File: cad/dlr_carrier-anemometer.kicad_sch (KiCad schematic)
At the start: 9 parts, among them J13 ANEMO_M12_5P, U7 SP3485EN

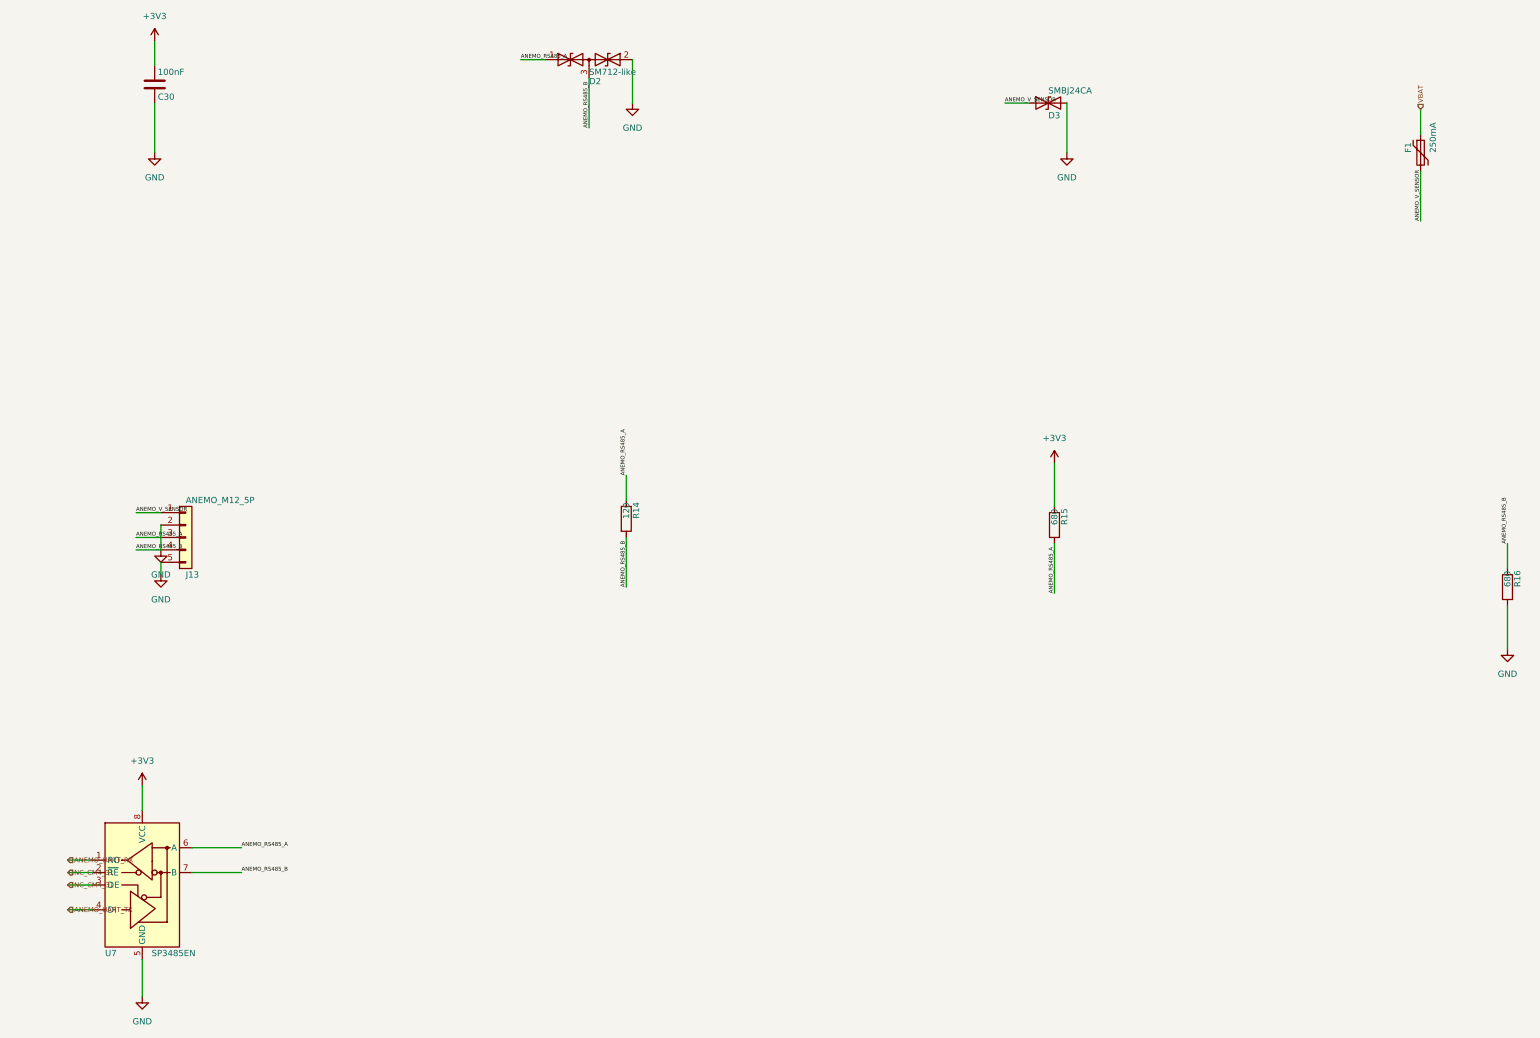
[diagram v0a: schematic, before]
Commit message: 🗺 feat(cad): scripted schematic + board pipeline, 4-layer stack
The committed board had almost every pad on +3V3 — no 5V_RAIL, VBAT or SDA1 net
existed on it at all — so the gerbers in output/ were never a valid board. Cause:
"Update PCB from Schematic" is GUI-only, so nothing kept the board honest, and the
schematic generator itself was merging nets.

Schematic generator:
  * power stubs now run along the pin direction; they used to be forced up or down
    regardless, which drove a 5V_RAIL stub straight through the buck inductor's
    BUCK_SW pin
  * PWR_FLAGs are placed by rule — any net that reaches a power-input pin with no
    power-output pin gets exactly one — instead of a hardcoded list, which is what
    the new VBAT and CHG_VCC rails needed
  * placement is deterministic; it used Python's salted hash(), so no two runs
    produced the same schematic
  * sch_guard fails the build on any cross-net wire/pin collision
  * ~700 lines of dead single-sheet generator removed
  ERC: 0 violations across all 8 sheets.

Board pipeline (cad/drawing/, all scripted, no GUI step):
  sync_pcb      rebuilds every footprint from the library and reassigns every pad
                net from the SKiDL netlist — the replacement for F8
  board_setup   4-layer SIG/GND/5V/SIG stack, rules, net classes, planes (ADR-016)
  route_pcb     DSN -> Freerouting -> SES, after patching the DSN so plane layers
                are "power" (the router was slicing the planes with signals) and
                the plane declarations are dropped (the router had been leaving
                GND and 5V pads with no path to the plane at all)
  stitch_planes vias from surface pads into their plane
  close_gaps    closes what the router leaves, using real segment-to-segment
                clearance; it never forces copper through another net

DRC: 265 unconnected -> 5, with no clearance, short, annular-ring or courtyard
errors. The remaining 5 are escapes on the DF40, the VQFN and the MSOP; they are
l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
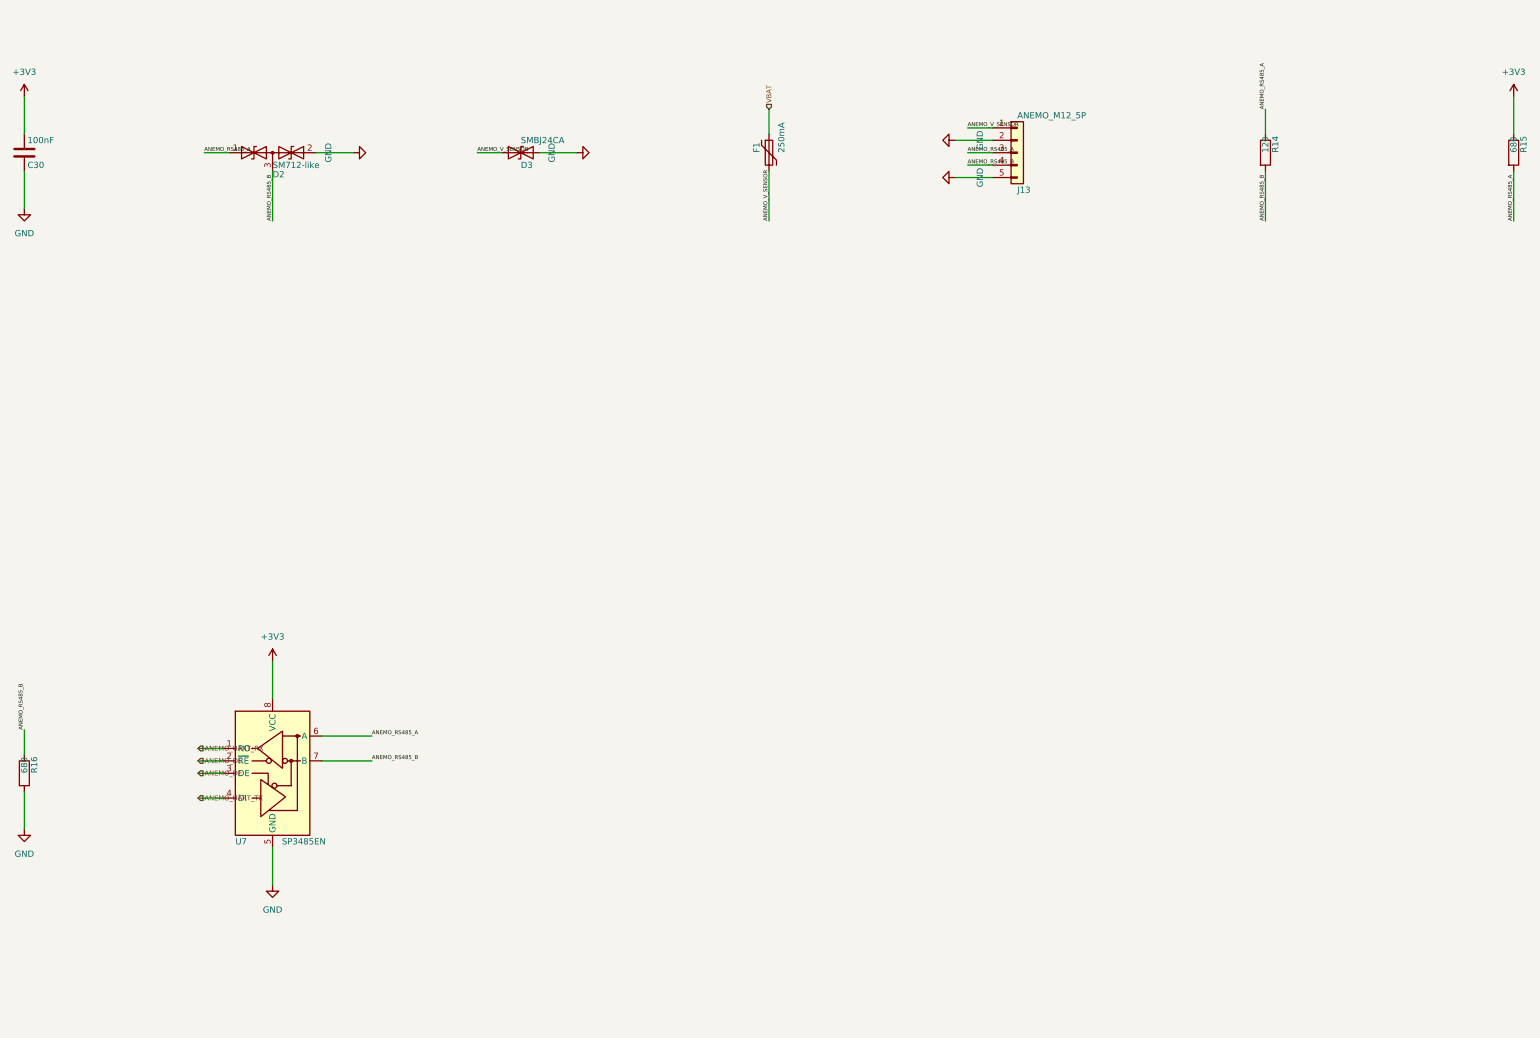
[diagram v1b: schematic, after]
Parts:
- D3: footprint Package_TO_SOT_SMD:SOT-23 -> Diode_SMD:D_SMB
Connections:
- net GND: no longer D2.3 (common), J13.4 (Pin_4), R14.2, R16.1, U7.7 (B)
- net NC_CM4_31 renamed ANEMO_DE
- new net ANEMO_RS485_B: D2.3 (common), J13.4 (Pin_4), R14.2, R16.1, U7.7 (B)

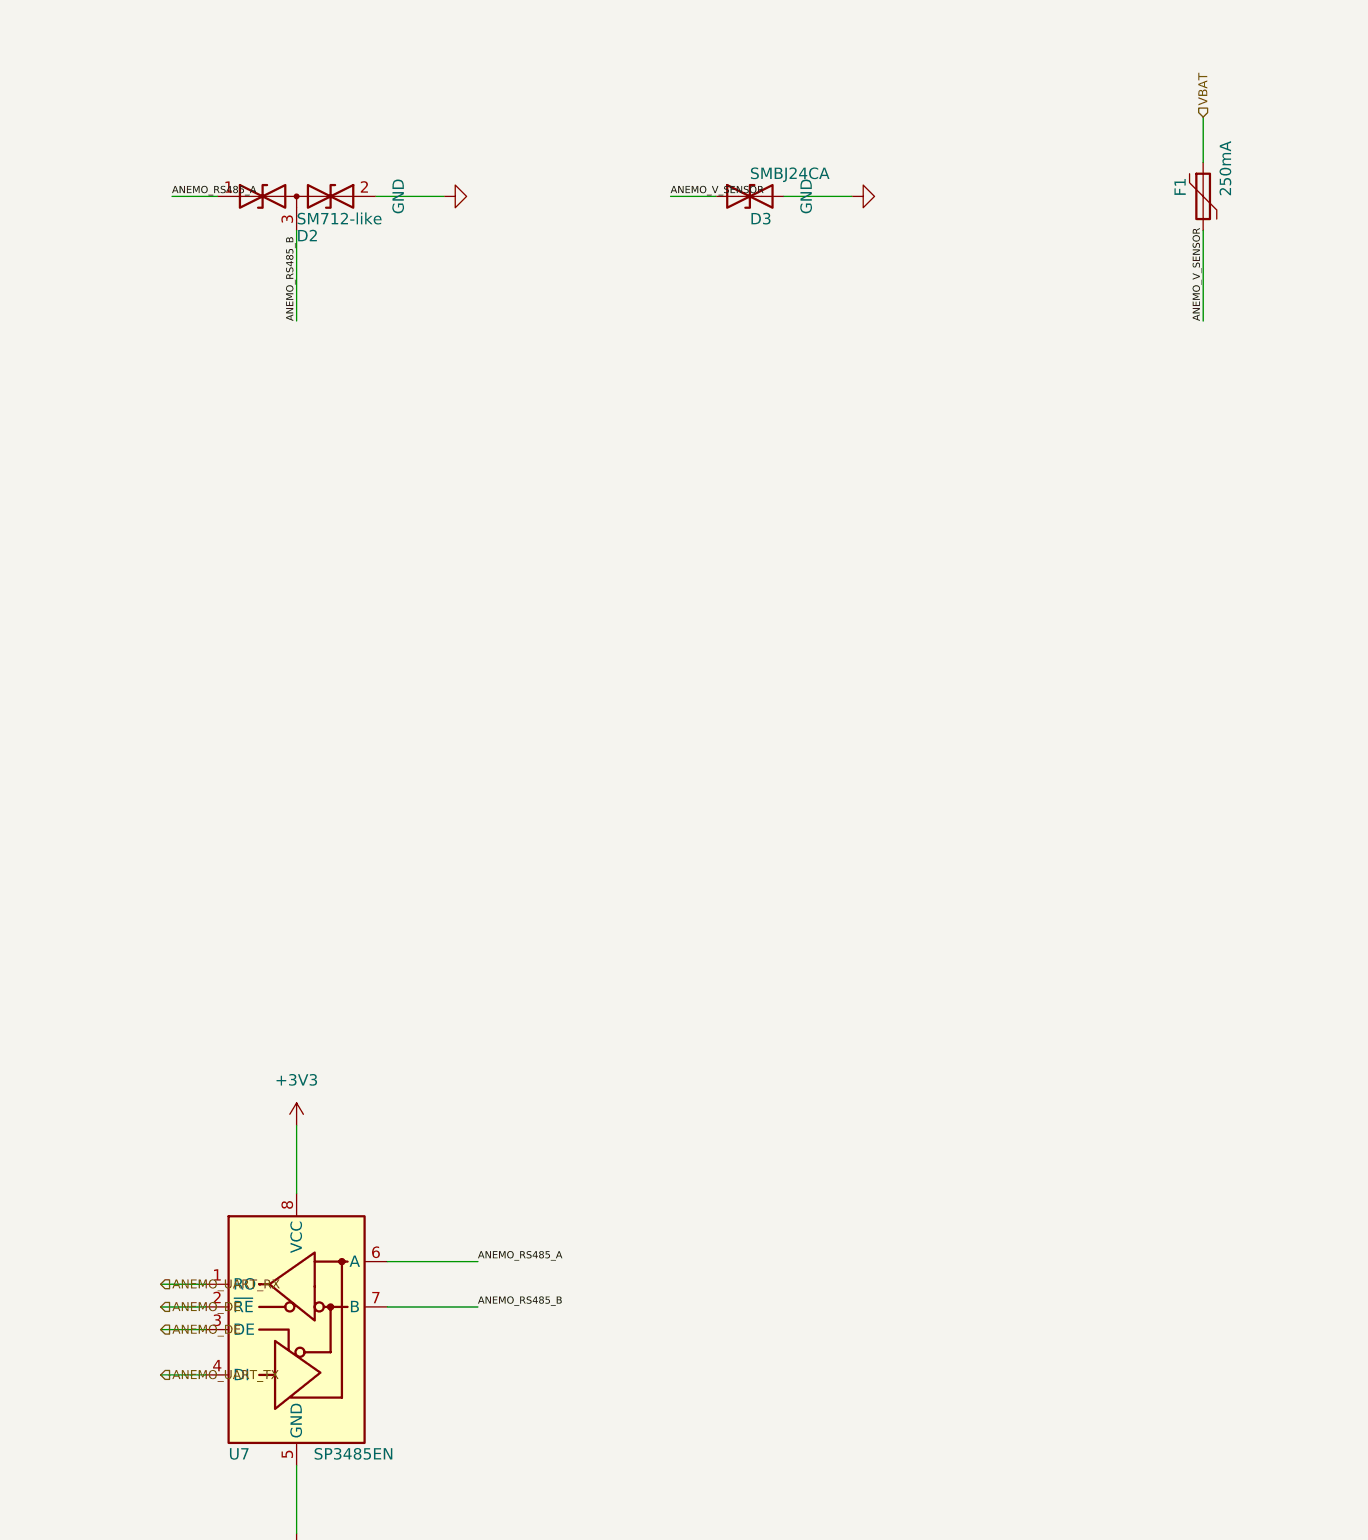
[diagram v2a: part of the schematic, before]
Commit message: 🩺 fix(schematic): match hierarchical label type to the sheet pin
The 117 KiCad 9 errors were a type mismatch, not the hierarchy metadata: every
child hierarchical label was written as `(shape input)` while the root's sheet pins
are bidirectional. KiCad's hier_label_mismatch check compares electrical type as
well as name, so on KiCad 9 every cross-sheet net failed, and the root labels then
read as dangling. KiCad 10 tolerates the mismatch, which is why it passed here.

kicad-sch-api 0.5.6 accepts a shape argument on add_hierarchical_label and ignores
it — the third serialization bug worked around in this generator — so the shape is
rewritten in the saved sheet.

Co-Authored-By: Claude Opus 5 <noreply@anthropic.com>
Claude-Session: https://claude.ai/code/session_011xr7VCL7rkJj2WE2uQF7sF
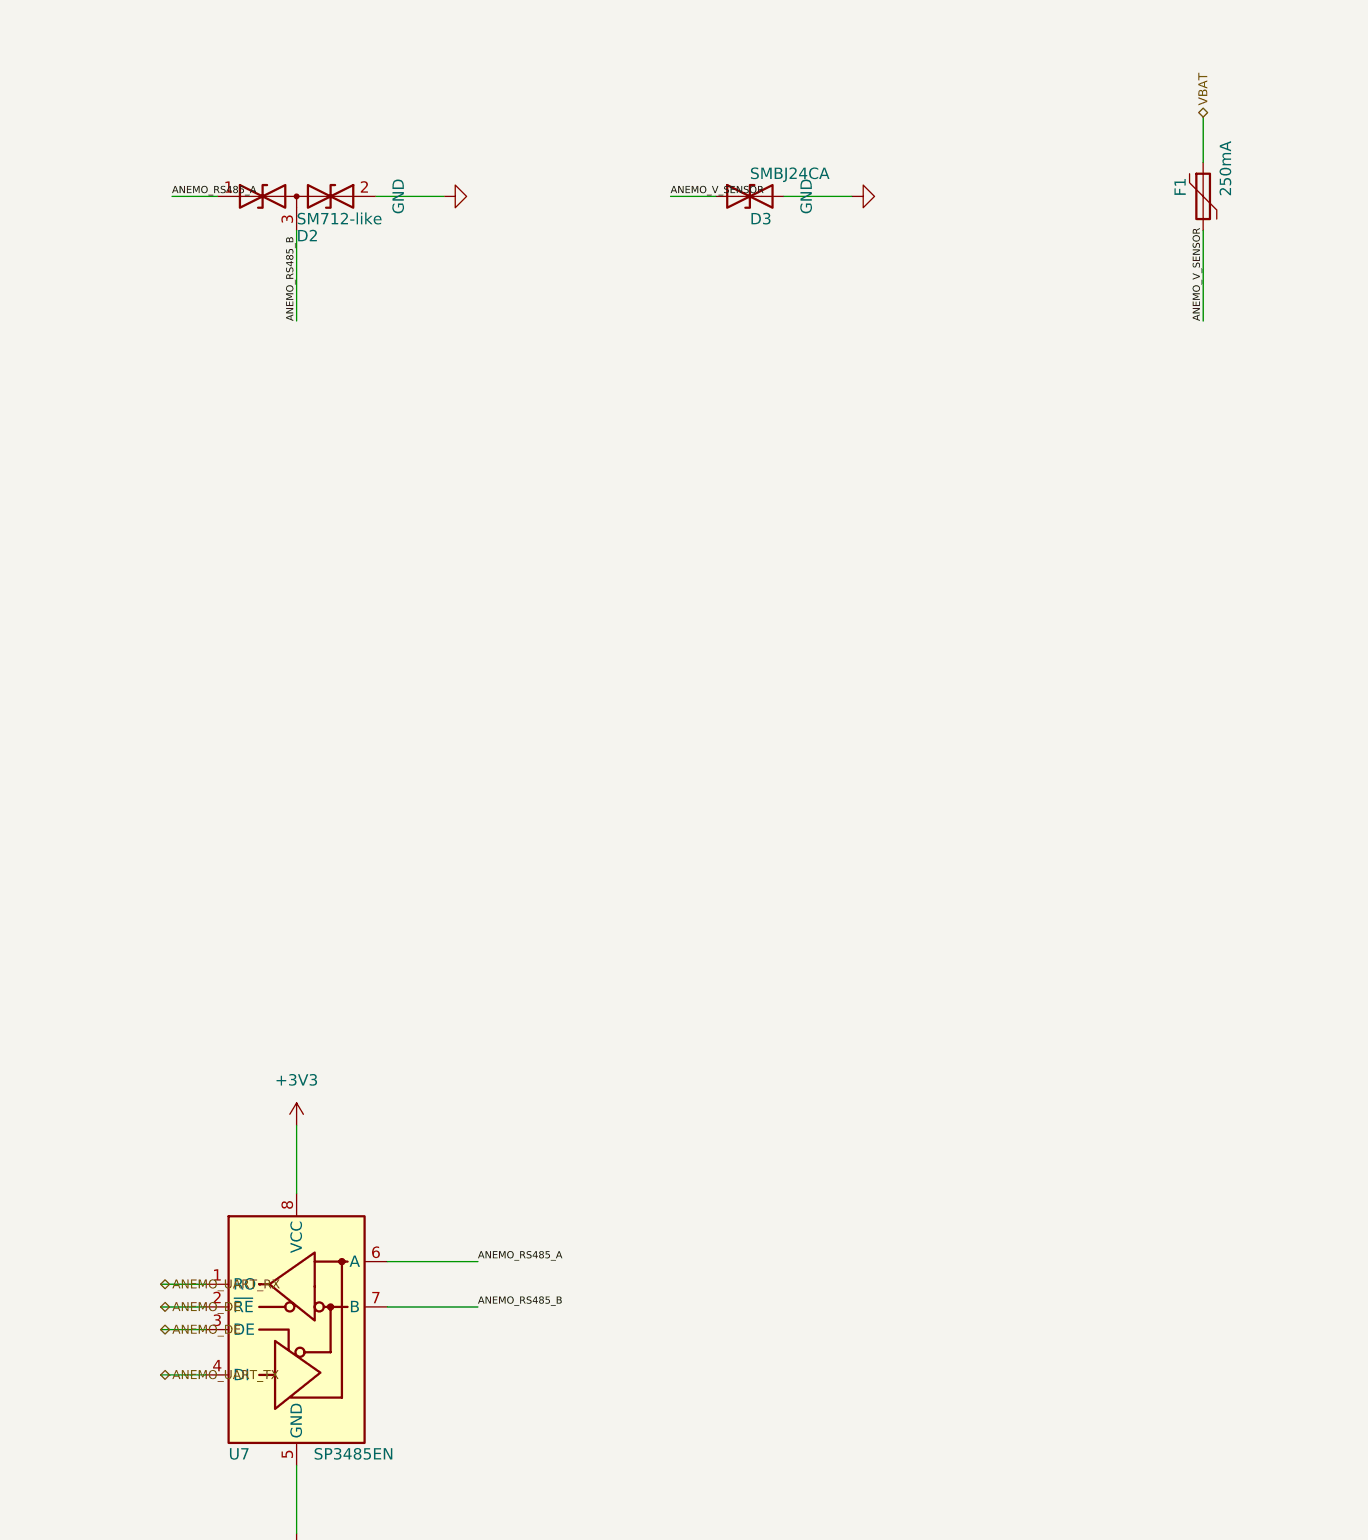
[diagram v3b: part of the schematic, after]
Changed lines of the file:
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@@
 		(instances
 			(project "ANEMOMETER RS-485"
-				(path "/006f20aa-e6de-45ca-869a-804cb883c933"
+				(path "/6472ff61-5240-4a8c-a1e1-c967d2308f1e"
 					(reference "C30")
 					(unit 1)
@@
 		(instances
 			(project "ANEMOMETER RS-485"
-				(path "/006f20aa-e6de-45ca-869a-804cb883c933"
+				(path "/6472ff61-5240-4a8c-a1e1-c967d2308f1e"
 					(reference "D2")
 					(unit 1)
@@
 		(instances
 			(project "ANEMOMETER RS-485"
-				(path "/006f20aa-e6de-45ca-869a-804cb883c933"
+				(path "/6472ff61-5240-4a8c-a1e1-c967d2308f1e"
 					(reference "D3")
 					(unit 1)
@@
 		(instances
 			(project "ANEMOMETER RS-485"
-				(path "/006f20aa-e6de-45ca-869a-804cb883c933"
+				(path "/6472ff61-5240-4a8c-a1e1-c967d2308f1e"
 					(reference "F1")
 					(unit 1)
@@
 		(instances
 			(project "ANEMOMETER RS-485"
-				(path "/006f20aa-e6de-45ca-869a-804cb883c933"
+				(path "/6472ff61-5240-4a8c-a1e1-c967d2308f1e"
 					(reference "J13")
 					(unit 1)
@@
 		(instances
 			(project "ANEMOMETER RS-485"
-				(path "/006f20aa-e6de-45ca-869a-804cb883c933"
+				(path "/6472ff61-5240-4a8c-a1e1-c967d2308f1e"
 					(reference "R14")
 					(unit 1)
@@
 		(instances
 			(project "ANEMOMETER RS-485"
-				(path "/006f20aa-e6de-45ca-869a-804cb883c933"
+				(path "/6472ff61-5240-4a8c-a1e1-c967d2308f1e"
 					(reference "R15")
 					(unit 1)
@@
 		(instances
 			(project "ANEMOMETER RS-485"
-				(path "/006f20aa-e6de-45ca-869a-804cb883c933"
+				(path "/6472ff61-5240-4a8c-a1e1-c967d2308f1e"
 					(reference "R16")
 					(unit 1)
@@
 		(instances
 			(project "ANEMOMETER RS-485"
-				(path "/006f20aa-e6de-45ca-869a-804cb883c933"
+				(path "/6472ff61-5240-4a8c-a1e1-c967d2308f1e"
 					(reference "U7")
 					(unit 1)
@@
 		(instances
 			(project "ANEMOMETER RS-485"
-				(path "/006f20aa-e6de-45ca-869a-804cb883c933"
+				(path "/6472ff61-5240-4a8c-a1e1-c967d2308f1e"
 					(reference "#PWR001")
 					(unit 1)
@@
 		(instances
 			(project "ANEMOMETER RS-485"
-				(path "/006f20aa-e6de-45ca-869a-804cb883c933"
+				(path "/6472ff61-5240-4a8c-a1e1-c967d2308f1e"
 					(reference "#PWR002")
 					(unit 1)
@@
 		(instances
 			(project "ANEMOMETER RS-485"
-				(path "/006f20aa-e6de-45ca-869a-804cb883c933"
+				(path "/6472ff61-5240-4a8c-a1e1-c967d2308f1e"
 					(reference "#PWR003")
 					(unit 1)
@@
 		(instances
 			(project "ANEMOMETER RS-485"
-				(path "/006f20aa-e6de-45ca-869a-804cb883c933"
+				(path "/6472ff61-5240-4a8c-a1e1-c967d2308f1e"
 					(reference "#PWR004")
 					(unit 1)
@@
 		(instances
 			(project "ANEMOMETER RS-485"
-				(path "/006f20aa-e6de-45ca-869a-804cb883c933"
+				(path "/6472ff61-5240-4a8c-a1e1-c967d2308f1e"
 					(reference "#PWR005")
 					(unit 1)
@@
 		(instances
 			(project "ANEMOMETER RS-485"
-				(path "/006f20aa-e6de-45ca-869a-804cb883c933"
+				(path "/6472ff61-5240-4a8c-a1e1-c967d2308f1e"
 					(reference "#PWR006")
 					(unit 1)
@@
 		(instances
 			(project "ANEMOMETER RS-485"
-				(path "/006f20aa-e6de-45ca-869a-804cb883c933"
+				(path "/6472ff61-5240-4a8c-a1e1-c967d2308f1e"
 					(reference "#PWR007")
 					(unit 1)
@@
 		(instances
 			(project "ANEMOMETER RS-485"
-				(path "/006f20aa-e6de-45ca-869a-804cb883c933"
+				(path "/6472ff61-5240-4a8c-a1e1-c967d2308f1e"
 					(reference "#PWR008")
 					(unit 1)
@@
 		(instances
 			(project "ANEMOMETER RS-485"
-				(path "/006f20aa-e6de-45ca-869a-804cb883c933"
+				(path "/6472ff61-5240-4a8c-a1e1-c967d2308f1e"
 					(reference "#PWR009")
 					(unit 1)
@@
 		(instances
 			(project "ANEMOMETER RS-485"
-				(path "/006f20aa-e6de-45ca-869a-804cb883c933"
+				(path "/6472ff61-5240-4a8c-a1e1-c967d2308f1e"
 					(reference "#PWR010")
 					(unit 1)
@@
 	)
 	(hierarchical_label "ANEMO_DE"
-		(shape input)
+		(shape bidirectional)
 		(at 99.06 226.06 180)
 		(effects
@@
 	)
 	(hierarchical_label "ANEMO_DE"
-		(shape input)
+		(shape bidirectional)
 		(at 99.06 228.6 180)
 		(effects
@@
 	)
 	(hierarchical_label "ANEMO_UART_RX"
-		(shape input)
+		(shape bidirectional)
 		(at 99.06 223.52 180)
 		(effects
@@
 	)
 	(hierarchical_label "ANEMO_UART_TX"
-		(shape input)
+		(shape bidirectional)
 		(at 99.06 233.68 180)
 		(effects
@@
 	)
 	(hierarchical_label "VBAT"
-		(shape input)
+		(shape bidirectional)
 		(at 215.9 92.71 90)
 		(effects
@@
 	)
 	(sheet_instances
-		(path "/64c7dfcb-bbfe-4df6-be89-9cb123185c21"
+		(path "/e3ea6974-3a36-4b21-b0e6-499ff9f9e43f"
 			(page "8")
 		)
